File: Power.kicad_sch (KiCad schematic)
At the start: 93 parts, among them Q1 SI2323DS, U10 AMS1117-ADJ, U3 AMS1117-3.3, U4 AMS1117-3.3, U5 AMS1117-3.3, U7 TPS65131RGER, U8 TLV70212_SOT23-5, U9 TLV70212_SOT23-5

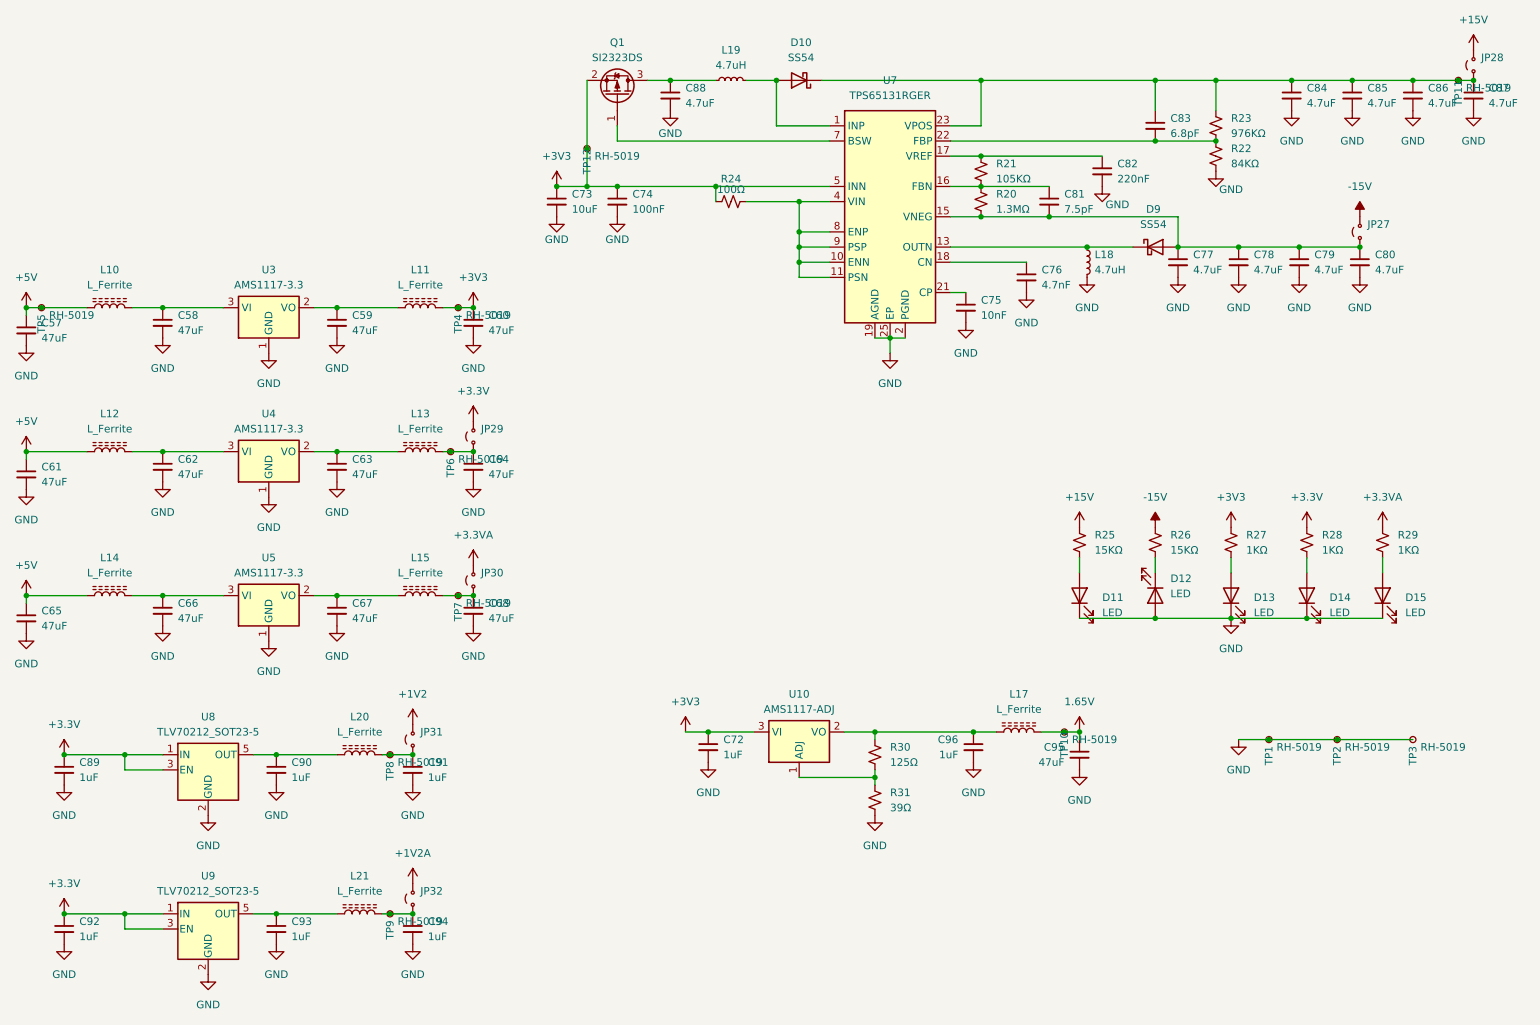
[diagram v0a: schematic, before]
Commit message: 1st test board manufacturing files
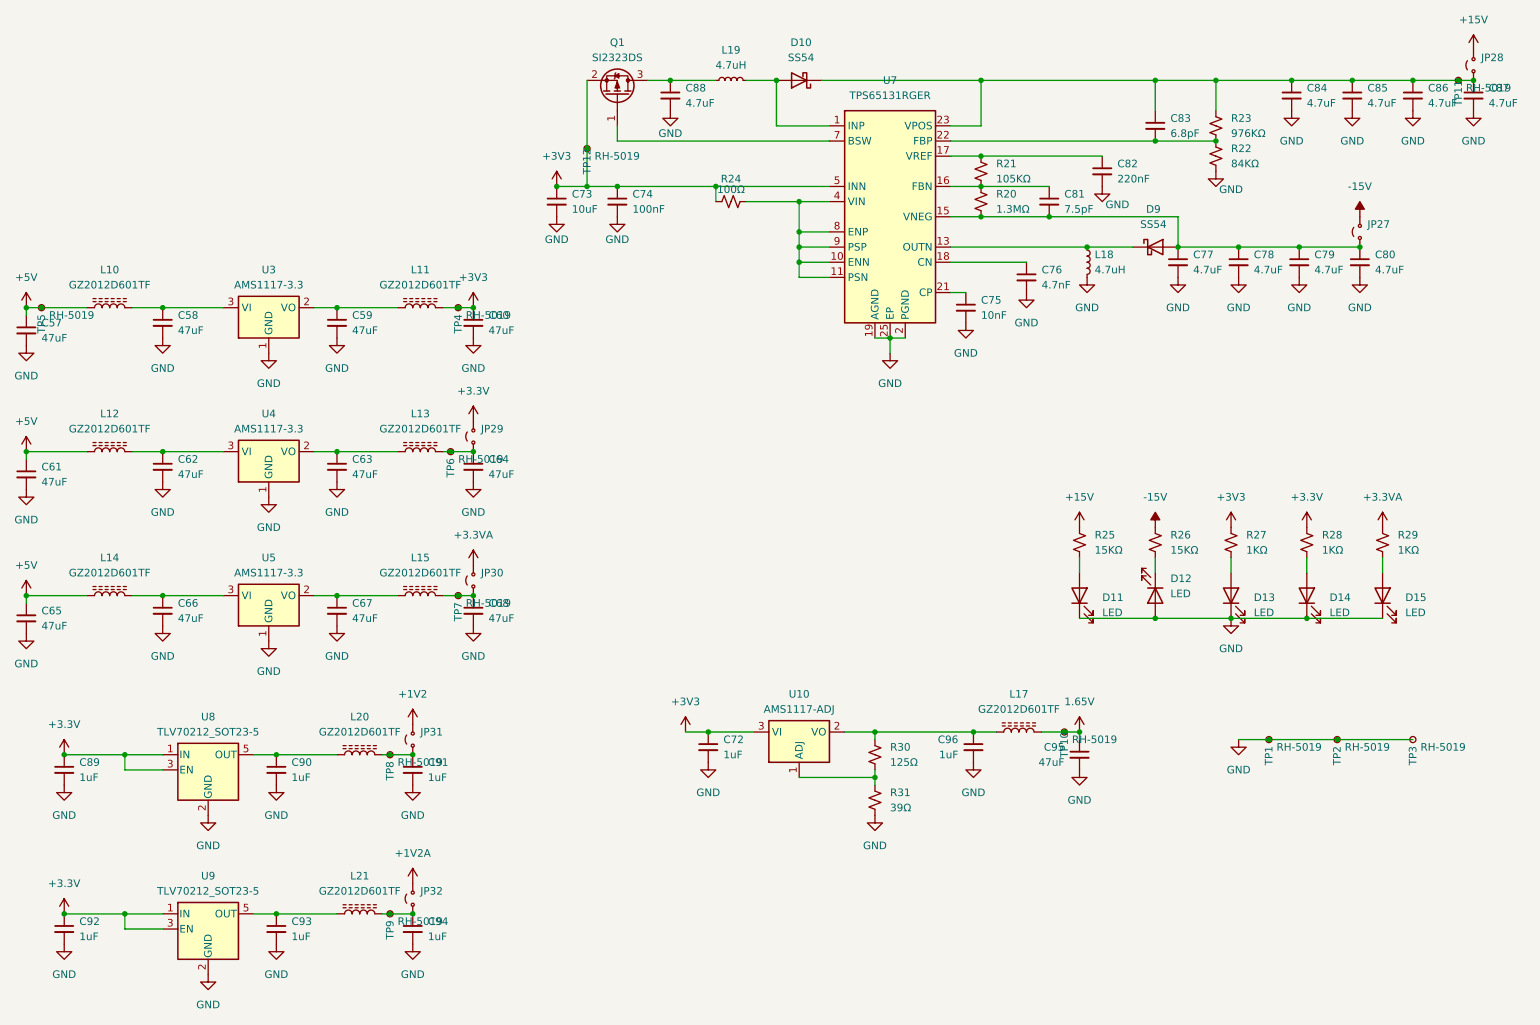
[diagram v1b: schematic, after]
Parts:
- L10, L11, L12, L13, L14, L15, L17, L20, L21: value L_Ferrite -> GZ2012D601TF
- R22: footprint Resistor_SMD:R_0805_2012Metric -> Resistor_SMD:R_0603_1608Metric; JLCPCB Part No # C2783077 -> C706010
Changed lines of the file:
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@@
 			)
 		)
-		(property "Footprint" "Resistor_SMD:R_0805_2012Metric"
+		(property "Footprint" "Resistor_SMD:R_0603_1608Metric"
 			(at 226.06 44.45 0)
 			(effects
@@
 			)
 		)
-		(property "JLCPCB Part No #" "C2783077"
+		(property "JLCPCB Part No #" "C706010"
 			(at 226.06 44.45 0)
 			(effects
@@
 			)
 		)
-		(property "Value" "L_Ferrite"
+		(property "Value" "GZ2012D601TF"
 			(at 193.04 137.16 90)
 			(effects
@@
 			)
 		)
-		(property "Value" "L_Ferrite"
+		(property "Value" "GZ2012D601TF"
 			(at 92.71 114.3 90)
 			(effects
@@
 			)
 		)
-		(property "Value" "L_Ferrite"
+		(property "Value" "GZ2012D601TF"
 			(at 92.71 90.17 90)
 			(effects
@@
 			)
 		)
-		(property "Value" "L_Ferrite"
+		(property "Value" "GZ2012D601TF"
 			(at 82.55 140.97 90)
 			(effects
@@
 			)
 		)
-		(property "Value" "L_Ferrite"
+		(property "Value" "GZ2012D601TF"
 			(at 40.64 66.04 90)
 			(effects
@@
 			)
 		)
-		(property "Value" "L_Ferrite"
+		(property "Value" "GZ2012D601TF"
 			(at 82.55 167.64 90)
 			(effects
@@
 			)
 		)
-		(property "Value" "L_Ferrite"
+		(property "Value" "GZ2012D601TF"
 			(at 40.64 90.17 90)
 			(effects
@@
 			)
 		)
-		(property "Value" "L_Ferrite"
+		(property "Value" "GZ2012D601TF"
 			(at 40.64 114.3 90)
 			(effects
@@
 			)
 		)
-		(property "Value" "L_Ferrite"
+		(property "Value" "GZ2012D601TF"
 			(at 92.71 66.04 90)
 			(effects
